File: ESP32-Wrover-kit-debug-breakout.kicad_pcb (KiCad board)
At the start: 2 copper layers, 85 x 83.1 mm, 6 parts, among them J101 Conn_02x14_Odd_Even, J102 Conn_02x09_Counter_Clockwise, J103 Conn_02x04_Odd_Even, J104 Conn_02x03_Odd_Even, J105 Conn_02x07_Odd_Even, J106 Conn_02x05_Odd_Even

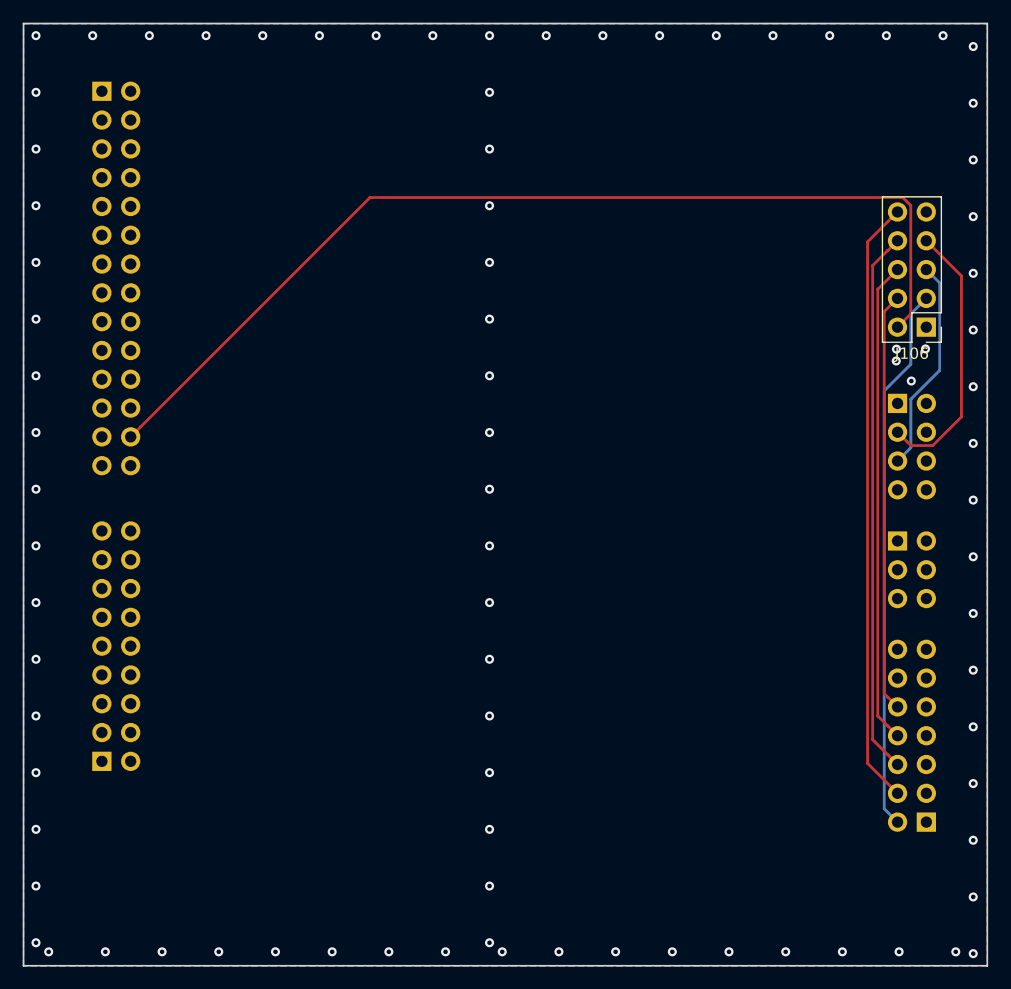
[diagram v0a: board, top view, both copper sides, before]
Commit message: Updated locations of headers.
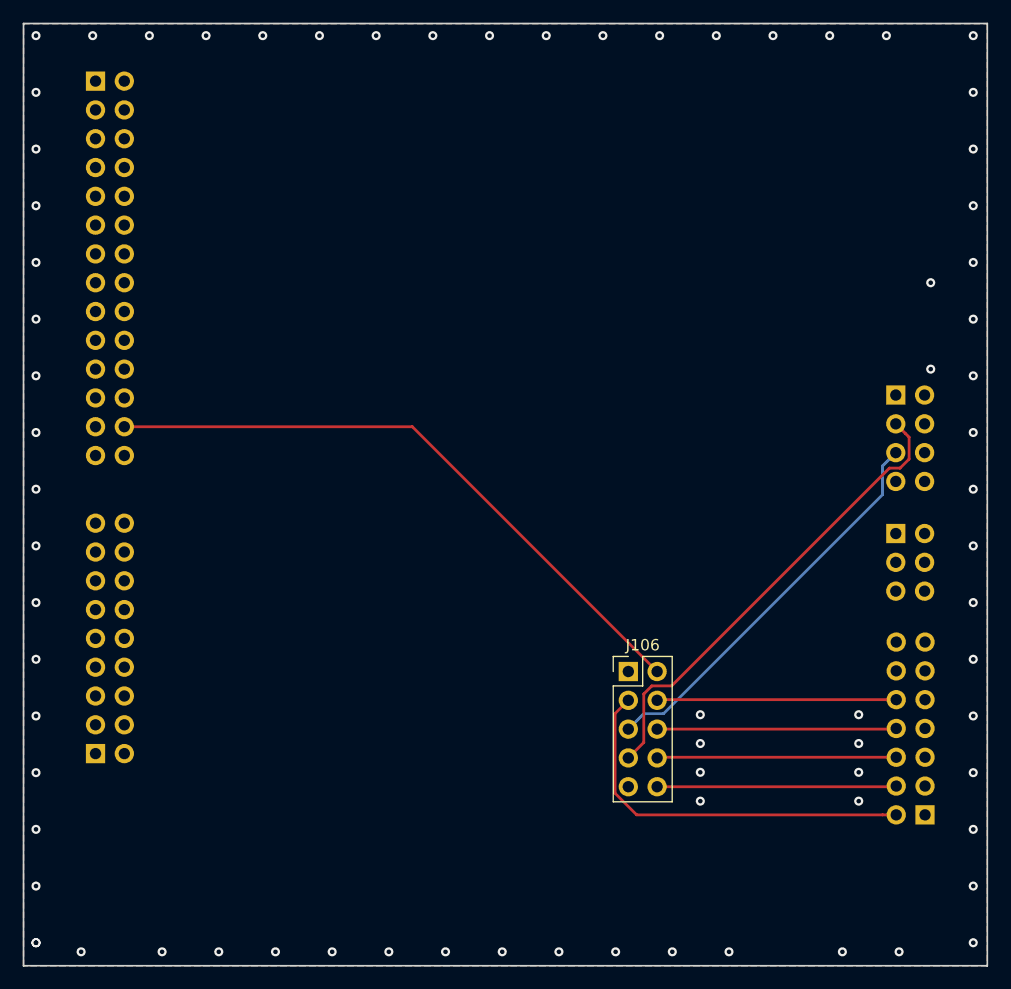
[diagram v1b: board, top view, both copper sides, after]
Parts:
- moved J106 40.2 mm to (103.3, 107.2), turned to 0 degrees
- moved J101 1.06 mm to (56.4, 55.1)
- moved J102 0.88 mm to (56.4, 114.4)
- moved J103 0.76 mm to (126.9, 82.8)
- moved J104 0.67 mm to (126.9, 95.0)
- moved J105 0.65 mm to (129.5, 119.8)
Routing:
- net /IO0_Boot_option: track 89.1 -> 55.9 mm
- net /MTMS: track 53.5 -> 21.1 mm
- net /MTDO: track 48.0 -> 21.1 mm
- net /MTDI: track 42.6 -> 21.1 mm
- net /RDX0: track 24.0 -> 41.8 mm
- net /TDX0: track 18.9 -> 35.2 mm
- net /MTCK: track 37.0 -> 21.1 mm
- net /CH_Enable: track 48.2 -> 34.3 mm
- net GND: vias 87 -> 74

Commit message: Text adjustements. Added PCB manufacturing files.
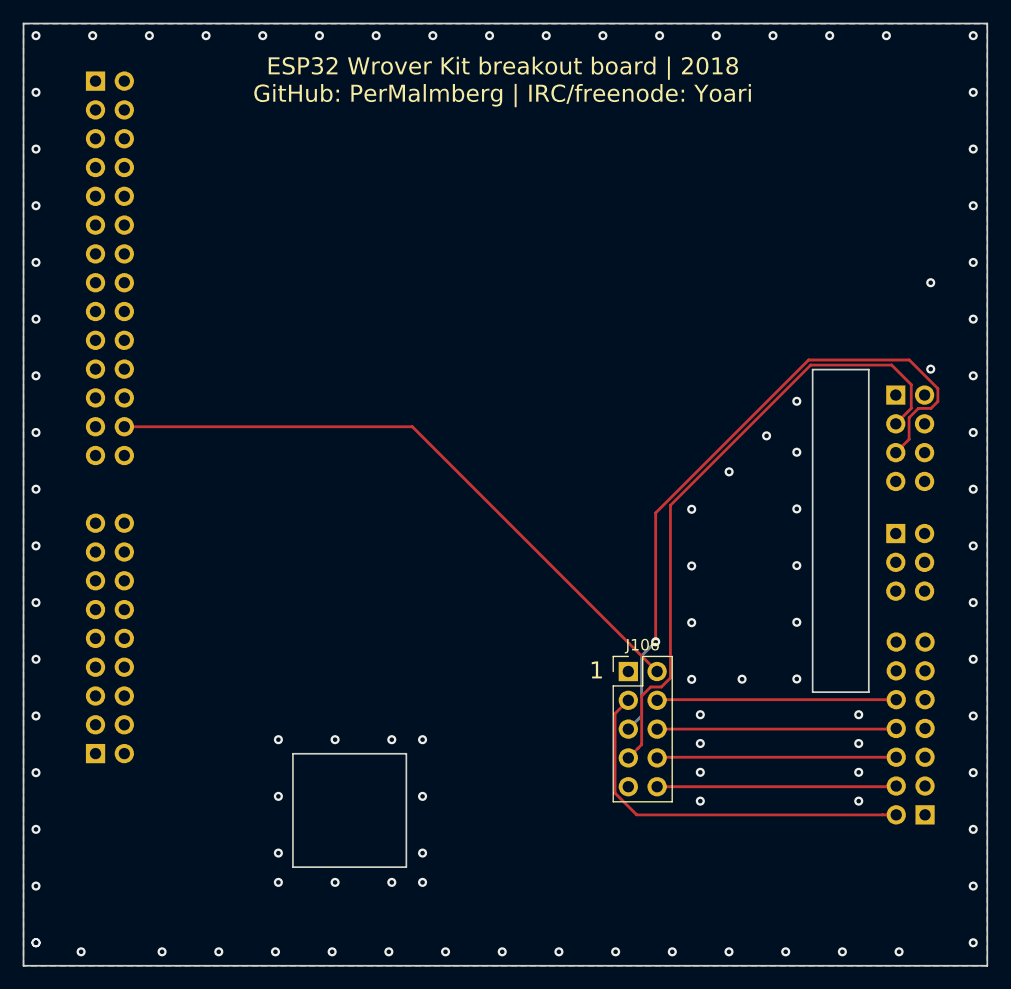
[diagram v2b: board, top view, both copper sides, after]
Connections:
- net /RDX0 renamed /RDX
- net /TDX0 renamed /TDX
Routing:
- net /TDX: track 35.2 -> 59.4 mm, vias 0 -> 1
- net /RDX: track 41.8 -> 55.5 mm
- net GND: vias 74 -> 100
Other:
- outline, holes or cut-outs redrawn
- board text added: "1"
- board text added: "ESP32 Wrover Kit breakout board | 2018 GitHub: PerMalmberg | IRC/freenode: Yoari"
- board text added: "JLCJLCJLCJLC"

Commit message: Fixed schematics. Closes #1. Closes #2
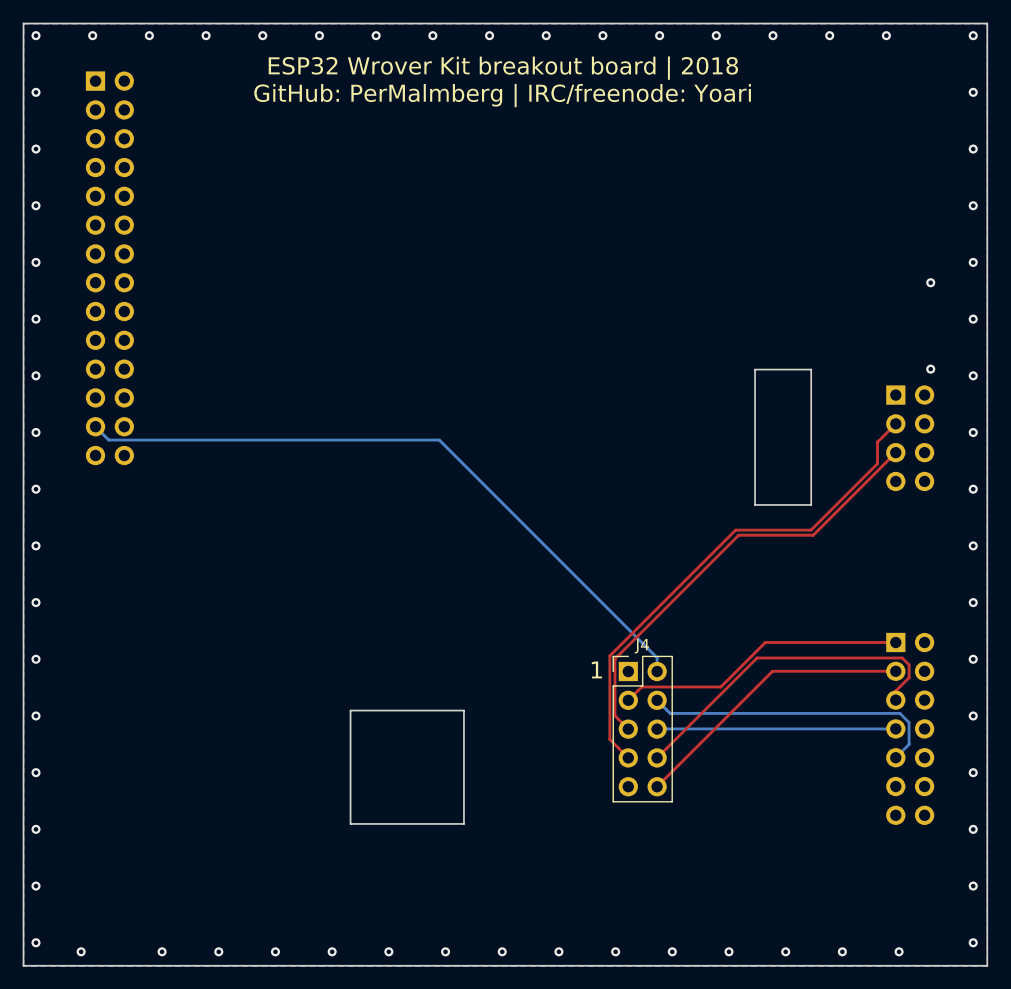
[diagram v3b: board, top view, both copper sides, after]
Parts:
- removed J102: Conn_02x09_Counter_Clockwise, Connector_PinHeader_2.54mm:PinHeader_2x09_P2.54mm_Vertical
- removed J104: Conn_02x03_Odd_Even, Connector_PinSocket_2.54mm:PinSocket_2x03_P2.54mm_Vertical
- moved J3 15.4 mm to (126.9, 104.6), turned to 180 degrees
- renumbered J101 to J1, J103 to J2, J105 to J3, J106 to J4
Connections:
- J1 pad 25: Net-(J101-Pad25) -> /IO0_Boot_option
- J1 pad 26: /IO0_Boot_option -> Net-(J1-Pad26)
- J3 pad 1: Net-(J105-Pad1) -> /CH_Enable
- J3 pad 10: /MTCK -> Net-(J3-Pad10)
- J3 pad 2: /CH_Enable -> Net-(J3-Pad2)
- J3 pad 3: Net-(J105-Pad3) -> /MTMS
- J3 pad 4: /MTMS -> Net-(J3-Pad4)
- J3 pad 5: Net-(J105-Pad5) -> /MTDO
- J3 pad 6: /MTDO -> Net-(J3-Pad6)
- J3 pad 7: Net-(J105-Pad7) -> /MTDI
- J3 pad 8: /MTDI -> Net-(J3-Pad8)
- J3 pad 9: Net-(J105-Pad9) -> /MTCK
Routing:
- net /TDX: track 59.4 -> 39.0 mm, vias 1 -> 0
- net /RDX: track 55.5 -> 44.5 mm
- net /MTDO: track 21.1 -> 29.7 mm
- net /CH_Enable: track 34.3 -> 25.7 mm
- net /MTCK: track 21.1 -> 26.6 mm
- net /MTMS: track 21.1 -> 25.3 mm
- net /IO0_Boot_option: track 55.9 -> 59.2 mm
- net GND: vias 100 -> 66
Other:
- outline, holes or cut-outs redrawn

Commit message: #2 Move JTAG signals to correct pin.
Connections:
- J3 pad 1: /CH_Enable -> Net-(J3-Pad1)
- J3 pad 10: Net-(J3-Pad10) -> /MTCK
- J3 pad 2: Net-(J3-Pad2) -> /CH_Enable
- J3 pad 3: /MTMS -> Net-(J3-Pad3)
- J3 pad 4: Net-(J3-Pad4) -> /MTMS
- J3 pad 5: /MTDO -> Net-(J3-Pad5)
- J3 pad 6: Net-(J3-Pad6) -> /MTDO
- J3 pad 7: /MTDI -> Net-(J3-Pad7)
- J3 pad 8: Net-(J3-Pad8) -> /MTDI
- J3 pad 9: /MTCK -> Net-(J3-Pad9)
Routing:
- net /MTDI: track 21.1 -> 34.1 mm
- net /MTCK: track 26.6 -> 35.2 mm
- net /MTMS: track 25.3 -> 31.3 mm
- net /CH_Enable: track 25.7 -> 29.2 mm
- net /MTDO: track 29.7 -> 26.7 mm
- net GND: vias 66 -> 76
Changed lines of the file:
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@@
     (thickness 1.6)
     (drawings 15)
-    (tracks 107)
+    (tracks 125)
     (zones 0)
     (modules 4)
@@
   (net 45 "Net-(J2-Pad8)")
   (net 46 "Net-(J4-Pad9)")
-  (net 47 "Net-(J3-Pad10)")
-  (net 48 "Net-(J3-Pad8)")
-  (net 49 "Net-(J3-Pad6)")
-  (net 50 "Net-(J3-Pad4)")
-  (net 51 "Net-(J3-Pad2)")
+  (net 47 "Net-(J3-Pad9)")
+  (net 48 "Net-(J3-Pad7)")
+  (net 49 "Net-(J3-Pad5)")
+  (net 50 "Net-(J3-Pad3)")
+  (net 51 "Net-(J3-Pad1)")
   (net_class Default "This is the default net class."
     (clearance 0.2)
@@
     (add_net "Net-(J2-Pad6)")
     (add_net "Net-(J2-Pad8)")
-    (add_net "Net-(J3-Pad10)")
+    (add_net "Net-(J3-Pad1)")
     (add_net "Net-(J3-Pad11)")
     (add_net "Net-(J3-Pad12)")
     (add_net "Net-(J3-Pad13)")
     (add_net "Net-(J3-Pad14)")
-    (add_net "Net-(J3-Pad2)")
-    (add_net "Net-(J3-Pad4)")
-    (add_net "Net-(J3-Pad6)")
-    (add_net "Net-(J3-Pad8)")
+    (add_net "Net-(J3-Pad3)")
+    (add_net "Net-(J3-Pad5)")
+    (add_net "Net-(J3-Pad7)")
+    (add_net "Net-(J3-Pad9)")
     (add_net "Net-(J4-Pad9)")
   )
@@
       (net 40 "Net-(J3-Pad11)"))
     (pad 10 thru_hole oval (at -2.54 -10.16 180) (size 1.7 1.7) (drill 1) (layers *.Cu *.Mask)
-      (net 47 "Net-(J3-Pad10)"))
+      (net 1 /MTCK))
     (pad 9 thru_hole oval (at 0 -10.16 180) (size 1.7 1.7) (drill 1) (layers *.Cu *.Mask)
-      (net 1 /MTCK))
+      (net 47 "Net-(J3-Pad9)"))
     (pad 8 thru_hole oval (at -2.54 -7.62 180) (size 1.7 1.7) (drill 1) (layers *.Cu *.Mask)
-      (net 48 "Net-(J3-Pad8)"))
+      (net 2 /MTDI))
     (pad 7 thru_hole oval (at 0 -7.62 180) (size 1.7 1.7) (drill 1) (layers *.Cu *.Mask)
-      (net 2 /MTDI))
+      (net 48 "Net-(J3-Pad7)"))
     (pad 6 thru_hole oval (at -2.54 -5.08 180) (size 1.7 1.7) (drill 1) (layers *.Cu *.Mask)
-      (net 49 "Net-(J3-Pad6)"))
+      (net 3 /MTDO))
     (pad 5 thru_hole oval (at 0 -5.08 180) (size 1.7 1.7) (drill 1) (layers *.Cu *.Mask)
-      (net 3 /MTDO))
+      (net 49 "Net-(J3-Pad5)"))
     (pad 4 thru_hole oval (at -2.54 -2.54 180) (size 1.7 1.7) (drill 1) (layers *.Cu *.Mask)
-      (net 50 "Net-(J3-Pad4)"))
+      (net 4 /MTMS))
     (pad 3 thru_hole oval (at 0 -2.54 180) (size 1.7 1.7) (drill 1) (layers *.Cu *.Mask)
-      (net 4 /MTMS))
+      (net 50 "Net-(J3-Pad3)"))
     (pad 2 thru_hole oval (at -2.54 0 180) (size 1.7 1.7) (drill 1) (layers *.Cu *.Mask)
-      (net 51 "Net-(J3-Pad2)"))
+      (net 6 /CH_Enable))
     (pad 1 thru_hole rect (at 0 0 180) (size 1.7 1.7) (drill 1) (layers *.Cu *.Mask)
-      (net 6 /CH_Enable))
+      (net 51 "Net-(J3-Pad1)"))
     (model ${KISYS3DMOD}/Connector_PinSocket_2.54mm.3dshapes/PinSocket_2x07_P2.54mm_Vertical.wrl
       (at (xyz 0 0 0))
@@
   (gr_line (start 50 50) (end 50 133.1) (layer Edge.Cuts) (width 0.15))
   (gr_line (start 50 50) (end 135 50) (layer Edge.Cuts) (width 0.15))
-  (segment (start 106.729999 110.539999) (end 105.88 109.69) (width 0.25) (layer B.Cu) (net 1))
-  (segment (start 107.037001 110.847001) (end 106.729999 110.539999) (width 0.25) (layer B.Cu) (net 1))
-  (segment (start 127.303003 110.847001) (end 107.037001 110.847001) (width 0.25) (layer B.Cu) (net 1))
-  (segment (start 128.104001 113.576999) (end 128.104001 111.647999) (width 0.25) (layer B.Cu) (net 1))
-  (segment (start 128.104001 111.647999) (end 127.303003 110.847001) (width 0.25) (layer B.Cu) (net 1))
-  (segment (start 126.929 114.752) (end 128.104001 113.576999) (width 0.25) (layer B.Cu) (net 1))
-  (segment (start 105.898 112.212) (end 105.88 112.23) (width 0.25) (layer B.Cu) (net 2))
-  (segment (start 126.929 112.212) (end 105.898 112.212) (width 0.25) (layer B.Cu) (net 2))
+  (segment (start 105.030001 110.539999) (end 105.88 109.69) (width 0.25) (layer F.Cu) (net 1))
+  (segment (start 104.704999 110.865001) (end 105.030001 110.539999) (width 0.25) (layer F.Cu) (net 1))
+  (segment (start 104.704999 117.874001) (end 104.704999 110.865001) (width 0.25) (layer F.Cu) (net 1))
+  (segment (start 105.315999 118.485001) (end 104.704999 117.874001) (width 0.25) (layer F.Cu) (net 1))
+  (segment (start 106.444001 118.485001) (end 105.315999 118.485001) (width 0.25) (layer F.Cu) (net 1))
+  (segment (start 109.002001 115.927001) (end 106.444001 118.485001) (width 0.25) (layer F.Cu) (net 1))
+  (segment (start 128.293999 115.927001) (end 109.002001 115.927001) (width 0.25) (layer F.Cu) (net 1))
+  (segment (start 129.469 114.752) (end 128.293999 115.927001) (width 0.25) (layer F.Cu) (net 1))
+  (segment (start 106.729999 111.380001) (end 105.88 112.23) (width 0.25) (layer F.Cu) (net 2))
+  (segment (start 112.153001 105.956999) (end 106.729999 111.380001) (width 0.25) (layer F.Cu) (net 2))
+  (segment (start 130.033001 105.956999) (end 112.153001 105.956999) (width 0.25) (layer F.Cu) (net 2))
+  (segment (start 131.094011 107.018009) (end 130.033001 105.956999) (width 0.25) (layer F.Cu) (net 2))
+  (segment (start 131.094011 110.586989) (end 131.094011 107.018009) (width 0.25) (layer F.Cu) (net 2))
+  (segment (start 129.469 112.212) (end 131.094011 110.586989) (width 0.25) (layer F.Cu) (net 2))
+  (segment (start 128.293999 108.496999) (end 112.153001 108.496999) (width 0.25) (layer F.Cu) (net 3))
   (segment (start 106.729999 113.920001) (end 105.88 114.77) (width 0.25) (layer F.Cu) (net 3))
-  (segment (start 114.693001 105.956999) (end 106.729999 113.920001) (width 0.25) (layer F.Cu) (net 3))
-  (segment (start 127.493001 105.956999) (end 114.693001 105.956999) (width 0.25) (layer F.Cu) (net 3))
-  (segment (start 128.104001 107.696001) (end 128.104001 106.567999) (width 0.25) (layer F.Cu) (net 3))
-  (segment (start 126.929 108.871002) (end 128.104001 107.696001) (width 0.25) (layer F.Cu) (net 3))
-  (segment (start 128.104001 106.567999) (end 127.493001 105.956999) (width 0.25) (layer F.Cu) (net 3))
-  (segment (start 126.929 109.672) (end 126.929 108.871002) (width 0.25) (layer F.Cu) (net 3))
-  (segment (start 116.058 107.132) (end 105.88 117.31) (width 0.25) (layer F.Cu) (net 4))
-  (segment (start 126.929 107.132) (end 116.058 107.132) (width 0.25) (layer F.Cu) (net 4))
+  (segment (start 112.153001 108.496999) (end 106.729999 113.920001) (width 0.25) (layer F.Cu) (net 3))
+  (segment (start 129.469 109.672) (end 128.293999 108.496999) (width 0.25) (layer F.Cu) (net 3))
+  (segment (start 106.729999 116.460001) (end 105.88 117.31) (width 0.25) (layer F.Cu) (net 4))
+  (segment (start 130.644001 110.236001) (end 129.843003 111.036999) (width 0.25) (layer F.Cu) (net 4))
+  (segment (start 130.644001 108.307001) (end 130.644001 110.236001) (width 0.25) (layer F.Cu) (net 4))
+  (segment (start 112.153001 111.036999) (end 106.729999 116.460001) (width 0.25) (layer F.Cu) (net 4))
+  (segment (start 129.843003 111.036999) (end 112.153001 111.036999) (width 0.25) (layer F.Cu) (net 4))
+  (segment (start 129.469 107.132) (end 130.644001 108.307001) (width 0.25) (layer F.Cu) (net 4))
   (via (at 51.1 51.07) (size 0.8) (drill 0.4) (layers F.Cu B.Cu) (net 5))
   (via (at 56.1 51.07) (size 0.8) (drill 0.4) (layers F.Cu B.Cu) (net 5))
@@
   (via (at 130.01 80.48) (size 0.8) (drill 0.4) (layers F.Cu B.Cu) (net 5))
   (via (at 117.22 131.87) (size 0.8) (drill 0.4) (layers F.Cu B.Cu) (net 5))
+  (via (at 112.865 112.399) (size 0.8) (drill 0.4) (layers F.Cu B.Cu) (net 5))
+  (via (at 124.549 111.891) (size 0.8) (drill 0.4) (layers F.Cu B.Cu) (net 5))
+  (via (at 124.549 114.939) (size 0.8) (drill 0.4) (layers F.Cu B.Cu) (net 5))
+  (via (at 110.706 114.558) (size 0.8) (drill 0.4) (layers F.Cu B.Cu) (net 5))
+  (via (at 112.865 109.859) (size 0.8) (drill 0.4) (layers F.Cu B.Cu) (net 5))
+  (via (at 124.549 109.732) (size 0.8) (drill 0.4) (layers F.Cu B.Cu) (net 5))
+  (via (at 124.549 107.192) (size 0.8) (drill 0.4) (layers F.Cu B.Cu) (net 5))
+  (via (at 124.549 104.525) (size 0.8) (drill 0.4) (layers F.Cu B.Cu) (net 5))
+  (via (at 112.865 104.779) (size 0.8) (drill 0.4) (layers F.Cu B.Cu) (net 5))
+  (via (at 112.865 107.319) (size 0.8) (drill 0.4) (layers F.Cu B.Cu) (net 5))
   (segment (start 104.189999 108.840001) (end 103.34 109.69) (width 0.25) (layer F.Cu) (net 6))
   (segment (start 104.515001 108.514999) (end 104.189999 108.840001) (width 0.25) (layer F.Cu) (net 6))
-  (segment (start 111.498591 108.514999) (end 104.515001 108.514999) (width 0.25) (layer F.Cu) (net 6))
-  (segment (start 115.42159 104.592) (end 111.498591 108.514999) (width 0.25) (layer F.Cu) (net 6))
-  (segment (start 126.929 104.592) (end 115.42159 104.592) (width 0.25) (layer F.Cu) (net 6))
+  (segment (start 106.254003 108.514999) (end 104.515001 108.514999) (width 0.25) (layer F.Cu) (net 6))
+  (segment (start 111.352003 103.416999) (end 106.254003 108.514999) (width 0.25) (layer F.Cu) (net 6))
+  (segment (start 128.293999 103.416999) (end 111.352003 103.416999) (width 0.25) (layer F.Cu) (net 6))
+  (segment (start 129.469 104.592) (end 128.293999 103.416999) (width 0.25) (layer F.Cu) (net 6))
   (segment (start 57.199999 86.409999) (end 56.35 85.56) (width 0.25) (layer B.Cu) (net 7) (status 30))
   (segment (start 57.525001 86.735001) (end 57.199999 86.409999) (width 0.25) (layer B.Cu) (net 7) (status 20))
@@
     (connect_pads (clearance 0.508))
     (min_thickness 0.254)
-    (fill (arc_segments 16) (thermal_gap 0.508) (thermal_bridge_width 0.508))
+    (fill yes (arc_segments 16) (thermal_gap 0.508) (thermal_bridge_width 0.508))
     (polygon
       (pts
@@
     (connect_pads (clearance 0.508))
     (min_thickness 0.254)
-    (fill (arc_segments 16) (thermal_gap 0.508) (thermal_bridge_width 0.508))
+    (fill yes (arc_segments 16) (thermal_gap 0.508) (thermal_bridge_width 0.508))
     (polygon
       (pts
